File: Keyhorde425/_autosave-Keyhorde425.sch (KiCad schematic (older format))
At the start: 110 parts, among them J1 MX-NoLED, J2 USB_C_Receptacle_USB2.0, K1 MX-NoLED, M1 MX-NoLED, P1 MX-NoLED, Q1 MX-NoLED, SW1 SW_Push, T1 MX-NoLED, U1 ATmega32U4-AU, U2 MX-NoLED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

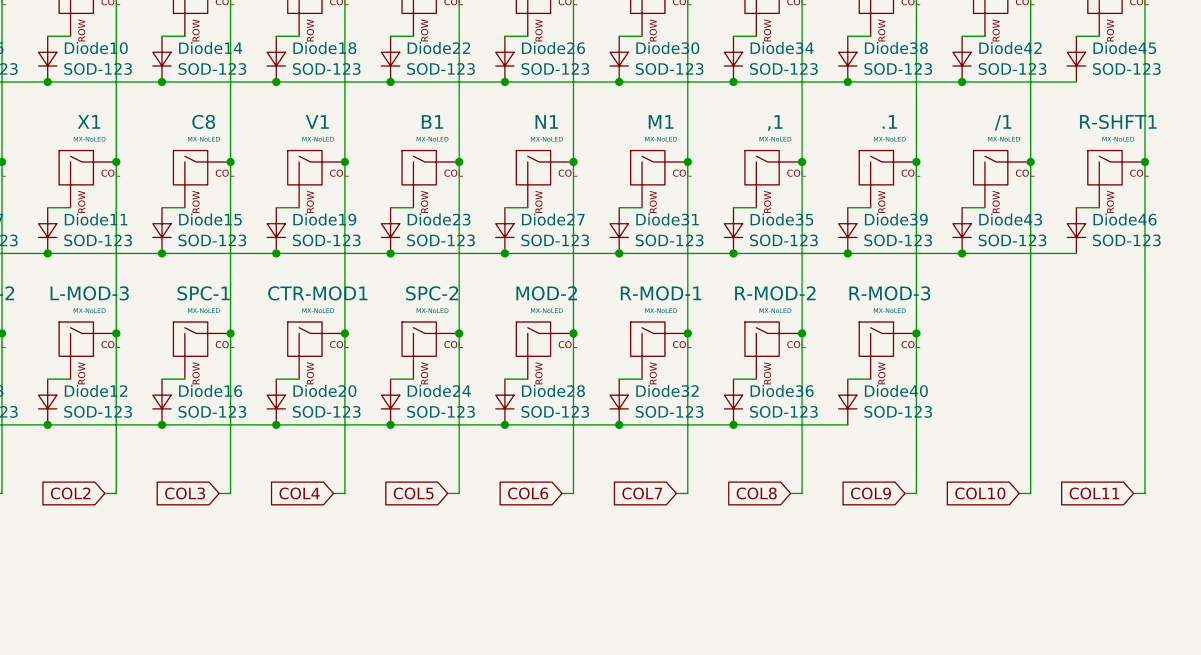
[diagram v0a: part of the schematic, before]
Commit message: Updated schematic with bad diode footprint
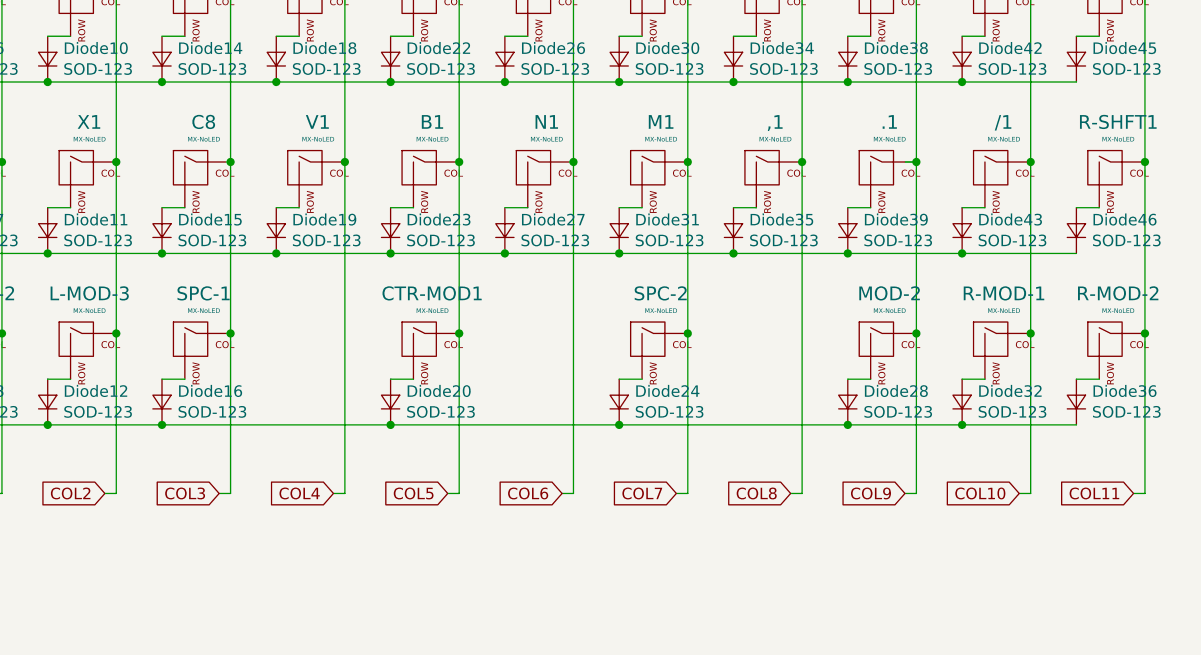
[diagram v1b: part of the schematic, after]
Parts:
- removed Diode40: SOD-123, Diode_THT:D_5KP_P7.62mm_Vertical_AnodeUp, symbol Device:D_Small
- removed R-MOD-3: MX-NoLED, MX_Alps_Hybrid:MX-1U, symbol MX_Alps_Hybrid:MX-NoLED
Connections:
- net COL10: now also R-MOD-1.1 (COL)
- net COL11: now also R-MOD-2.1 (COL)
- net COL4: no longer CTR-MOD1.1 (COL)
- net COL5: now also CTR-MOD1.1 (COL); no longer SPC-2.1 (COL)
- net COL6: no longer MOD-2.1 (COL)
- net COL7: now also SPC-2.1 (COL); no longer R-MOD-1.1 (COL)
- net COL8: no longer R-MOD-2.1 (COL)
- net COL9: now also MOD-2.1 (COL)
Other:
- moved on the sheet: CTR-MOD1, Diode20, Diode24, Diode28, Diode32, Diode36, MOD-2, R-MOD-1, R-MOD-2, SPC-2
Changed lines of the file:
@@
 L MX_Alps_Hybrid:MX-NoLED CTR-MOD1
 U 1 1 6388747C
-P 7250 4350
-F 0 "CTR-MOD1" H 7283 4573 60  0000 C CNN
-F 1 "MX-NoLED" H 7283 4499 20  0000 C CNN
-F 2 "MX_Alps_Hybrid:MX-1U" H 6625 4325 60  0001 C CNN
-F 3 "" H 6625 4325 60  0001 C CNN
-	1    7250 4350
-	1    0    0    -1
-$EndComp
-$Comp
-L Device:D_Small Diode20
-U 1 1 63887482
-P 7100 4600
-F 0 "Diode20" V 7146 4532 50  0000 R CNN
-F 1 "SOD-123" V 7055 4532 50  0000 R CNN
-F 2 "Diode_THT:D_5KP_P7.62mm_Vertical_AnodeUp" V 7100 4600 50  0001 C CNN
-F 3 "~" V 7100 4600 50  0001 C CNN
-	1    7100 4600
-	0    -1   -1   0
-$EndComp
-Wire Wire Line
-	7100 4500 7200 4500
-$Comp
-L MX_Alps_Hybrid:MX-NoLED SPC-2
-U 1 1 63887489
 P 7750 4350
-F 0 "SPC-2" H 7783 4573 60  0000 C CNN
+F 0 "CTR-MOD1" H 7783 4573 60  0000 C CNN
 F 1 "MX-NoLED" H 7783 4499 20  0000 C CNN
 F 2 "MX_Alps_Hybrid:MX-1U" H 7125 4325 60  0001 C CNN
@@
 $EndComp
 $Comp
-L Device:D_Small Diode24
-U 1 1 6388748F
+L Device:D_Small Diode20
+U 1 1 63887482
 P 7600 4600
-F 0 "Diode24" V 7646 4532 50  0000 R CNN
+F 0 "Diode20" V 7646 4532 50  0000 R CNN
 F 1 "SOD-123" V 7555 4532 50  0000 R CNN
 F 2 "Diode_THT:D_5KP_P7.62mm_Vertical_AnodeUp" V 7600 4600 50  0001 C CNN
@@
 	7600 4500 7700 4500
 $Comp
-L MX_Alps_Hybrid:MX-NoLED MOD-2
-U 1 1 63887496
-P 8250 4350
-F 0 "MOD-2" H 8283 4573 60  0000 C CNN
-F 1 "MX-NoLED" H 8283 4499 20  0000 C CNN
-F 2 "MX_Alps_Hybrid:MX-1U" H 7625 4325 60  0001 C CNN
-F 3 "" H 7625 4325 60  0001 C CNN
-	1    8250 4350
-	1    0    0    -1
-$EndComp
-$Comp
-L Device:D_Small Diode28
-U 1 1 6388749C
-P 8100 4600
-F 0 "Diode28" V 8146 4532 50  0000 R CNN
-F 1 "SOD-123" V 8055 4532 50  0000 R CNN
-F 2 "Diode_THT:D_5KP_P7.62mm_Vertical_AnodeUp" V 8100 4600 50  0001 C CNN
-F 3 "~" V 8100 4600 50  0001 C CNN
-	1    8100 4600
-	0    -1   -1   0
-$EndComp
-Wire Wire Line
-	8100 4500 8200 4500
-$Comp
-L MX_Alps_Hybrid:MX-NoLED R-MOD-1
-U 1 1 638874A3
+L MX_Alps_Hybrid:MX-NoLED SPC-2
+U 1 1 63887489
 P 8750 4350
-F 0 "R-MOD-1" H 8783 4573 60  0000 C CNN
+F 0 "SPC-2" H 8783 4573 60  0000 C CNN
 F 1 "MX-NoLED" H 8783 4499 20  0000 C CNN
 F 2 "MX_Alps_Hybrid:MX-1U" H 8125 4325 60  0001 C CNN
@@
 $EndComp
 $Comp
-L Device:D_Small Diode32
-U 1 1 638874A9
+L Device:D_Small Diode24
+U 1 1 6388748F
 P 8600 4600
-F 0 "Diode32" V 8646 4532 50  0000 R CNN
+F 0 "Diode24" V 8646 4532 50  0000 R CNN
 F 1 "SOD-123" V 8555 4532 50  0000 R CNN
 F 2 "Diode_THT:D_5KP_P7.62mm_Vertical_AnodeUp" V 8600 4600 50  0001 C CNN
@@
 	8600 4500 8700 4500
 $Comp
-L MX_Alps_Hybrid:MX-NoLED R-MOD-2
-U 1 1 638874B0
-P 9250 4350
-F 0 "R-MOD-2" H 9283 4573 60  0000 C CNN
-F 1 "MX-NoLED" H 9283 4499 20  0000 C CNN
-F 2 "MX_Alps_Hybrid:MX-1U" H 8625 4325 60  0001 C CNN
-F 3 "" H 8625 4325 60  0001 C CNN
-	1    9250 4350
-	1    0    0    -1
-$EndComp
-$Comp
-L Device:D_Small Diode36
-U 1 1 638874B6
-P 9100 4600
-F 0 "Diode36" V 9146 4532 50  0000 R CNN
-F 1 "SOD-123" V 9055 4532 50  0000 R CNN
-F 2 "Diode_THT:D_5KP_P7.62mm_Vertical_AnodeUp" V 9100 4600 50  0001 C CNN
-F 3 "~" V 9100 4600 50  0001 C CNN
-	1    9100 4600
-	0    -1   -1   0
-$EndComp
-Wire Wire Line
-	9100 4500 9200 4500
-$Comp
-L MX_Alps_Hybrid:MX-NoLED R-MOD-3
-U 1 1 638874BD
+L MX_Alps_Hybrid:MX-NoLED MOD-2
+U 1 1 63887496
 P 9750 4350
-F 0 "R-MOD-3" H 9783 4573 60  0000 C CNN
+F 0 "MOD-2" H 9783 4573 60  0000 C CNN
 F 1 "MX-NoLED" H 9783 4499 20  0000 C CNN
 F 2 "MX_Alps_Hybrid:MX-1U" H 9125 4325 60  0001 C CNN
@@
 $EndComp
 $Comp
-L Device:D_Small Diode40
-U 1 1 638874C3
+L Device:D_Small Diode28
+U 1 1 6388749C
 P 9600 4600
-F 0 "Diode40" V 9646 4532 50  0000 R CNN
+F 0 "Diode28" V 9646 4532 50  0000 R CNN
 F 1 "SOD-123" V 9555 4532 50  0000 R CNN
 F 2 "Diode_THT:D_5KP_P7.62mm_Vertical_AnodeUp" V 9600 4600 50  0001 C CNN
@@
 Wire Wire Line
 	9600 4500 9700 4500
+$Comp
+L MX_Alps_Hybrid:MX-NoLED R-MOD-1
+U 1 1 638874A3
+P 10250 4350
+F 0 "R-MOD-1" H 10283 4573 60  0000 C CNN
+F 1 "MX-NoLED" H 10283 4499 20  0000 C CNN
+F 2 "MX_Alps_Hybrid:MX-1U" H 9625 4325 60  0001 C CNN
+F 3 "" H 9625 4325 60  0001 C CNN
+	1    10250 4350
+	1    0    0    -1
+$EndComp
+$Comp
+L Device:D_Small Diode32
+U 1 1 638874A9
+P 10100 4600
+F 0 "Diode32" V 10146 4532 50  0000 R CNN
+F 1 "SOD-123" V 10055 4532 50  0000 R CNN
+F 2 "Diode_THT:D_5KP_P7.62mm_Vertical_AnodeUp" V 10100 4600 50  0001 C CNN
+F 3 "~" V 10100 4600 50  0001 C CNN
+	1    10100 4600
+	0    -1   -1   0
+$EndComp
+Wire Wire Line
+	10100 4500 10200 4500
 Wire Wire Line
 	5100 2450 5600 2450
@@
 Wire Wire Line
 	6100 4700 6600 4700
-Connection ~ 6600 4700
-Wire Wire Line
-	6600 4700 7100 4700
-Connection ~ 7100 4700
-Wire Wire Line
-	7100 4700 7600 4700
-Connection ~ 7600 4700
-Wire Wire Line
-	7600 4700 8100 4700
-Connection ~ 8100 4700
-Wire Wire Line
-	8100 4700 8600 4700
-Connection ~ 8600 4700
-Wire Wire Line
-	8600 4700 9100 4700
-Connection ~ 9100 4700
-Wire Wire Line
-	9100 4700 9600 4700
 Wire Wire Line
 	5400 2050 5400 2800
@@
 Wire Wire Line
 	7400 2800 7400 3550
-Connection ~ 7400 3550
-Wire Wire Line
-	7400 3550 7400 4300
 Wire Wire Line
 	7900 2050 7900 2800
@@
 Wire Wire Line
 	7900 2800 7900 3550
-Connection ~ 7900 3550
-Wire Wire Line
-	7900 3550 7900 4300
 Wire Wire Line
 	8400 2050 8400 2800
@@
 Wire Wire Line
 	8400 2800 8400 3550
-Connection ~ 8400 3550
-Wire Wire Line
-	8400 3550 8400 4300
 Wire Wire Line
 	8900 2050 8900 2800
@@
 Wire Wire Line
 	8900 2800 8900 3550
-Connection ~ 8900 3550
-Wire Wire Line
-	8900 3550 8900 4300
 Wire Wire Line
 	9400 2050 9400 2800
@@
 Wire Wire Line
 	9400 2800 9400 3550
-Connection ~ 9400 3550
-Wire Wire Line
-	9400 3550 9400 4300
 Wire Wire Line
 	9900 2050 9900 2800
@@
 Wire Wire Line
 	9900 2800 9900 3550
-Connection ~ 9900 3550
-Wire Wire Line
-	9900 3550 9900 4300
 Connection ~ 9100 2450
 Wire Wire Line
@@
 Connection ~ 6900 4300
 Wire Wire Line
-	7400 4300 7400 5000
-Wire Wire Line
 	7400 5000 7350 5000
-Connection ~ 7400 4300
-Wire Wire Line
-	7900 4300 7900 5000
 Wire Wire Line
 	7900 5000 7850 5000
-Connection ~ 7900 4300
-Wire Wire Line
-	8400 4300 8400 5000
 Wire Wire Line
 	8400 5000 8350 5000
-Connection ~ 8400 4300
-Wire Wire Line
-	8900 4300 8900 5000
 Wire Wire Line
 	8900 5000 8850 5000
-Connection ~ 8900 4300
-Wire Wire Line
-	9400 4300 9400 5000
 Wire Wire Line
 	9400 5000 9350 5000
-Connection ~ 9400 4300
-Wire Wire Line
-	9900 4300 9900 5000
 Wire Wire Line
 	9900 5000 9850 5000
-Connection ~ 9900 4300
-Wire Wire Line
-	10400 3550 10400 5000
+Wire Wire Line
+	10400 3550 10400 4300
 Wire Wire Line
 	10400 5000 10350 5000
 Connection ~ 10400 3550
-Wire Wire Line
-	10900 3550 10900 5000
 Wire Wire Line
 	10900 5000 10850 5000
@@
 Wire Wire Line
 	3600 3900 3850 3900
+Wire Wire Line
+	10900 3550 10900 4300
+Wire Wire Line
+	10600 4500 10700 4500
+$Comp
+L Device:D_Small Diode36
+U 1 1 638874B6
+P 10600 4600
+F 0 "Diode36" V 10646 4532 50  0000 R CNN
+F 1 "SOD-123" V 10555 4532 50  0000 R CNN
+F 2 "Diode_THT:D_5KP_P7.62mm_Vertical_AnodeUp" V 10600 4600 50  0001 C CNN
+F 3 "~" V 10600 4600 50  0001 C CNN
+	1    10600 4600
+	0    -1   -1   0
+$EndComp
+$Comp
+L MX_Alps_Hybrid:MX-NoLED R-MOD-2
+U 1 1 638874B0
+P 10750 4350
+F 0 "R-MOD-2" H 10783 4573 60  0000 C CNN
+F 1 "MX-NoLED" H 10783 4499 20  0000 C CNN
+F 2 "MX_Alps_Hybrid:MX-1U" H 10125 4325 60  0001 C CNN
+F 3 "" H 10125 4325 60  0001 C CNN
+	1    10750 4350
+	1    0    0    -1
+$EndComp
+Connection ~ 10900 4300
+Wire Wire Line
+	10900 4300 10900 5000
+Connection ~ 10400 4300
+Wire Wire Line
+	10400 4300 10400 5000
+Wire Wire Line
+	9850 3550 9900 3550
+Connection ~ 9900 3550
+Wire Wire Line
+	9900 3550 9900 4300
+Wire Wire Line
+	9900 4300 9900 5000
+Connection ~ 9900 4300
+Wire Wire Line
+	8900 3550 8900 4300
+Connection ~ 8900 3550
+Wire Wire Line
+	8900 4300 8900 5000
+Connection ~ 8900 4300
+Wire Wire Line
+	9400 3550 9400 5000
+Connection ~ 9400 3550
+Wire Wire Line
+	7900 3550 7900 4300
+Connection ~ 7900 3550
+Wire Wire Line
+	7900 4300 7900 5000
+Connection ~ 7900 4300
+Wire Wire Line
+	6600 4700 7600 4700
+Connection ~ 6600 4700
+Wire Wire Line
+	7600 4700 8600 4700
+Connection ~ 7600 4700
+Wire Wire Line
+	8600 4700 9600 4700
+Connection ~ 8600 4700
+Wire Wire Line
+	7400 3550 7400 5000
+Connection ~ 7400 3550
+Wire Wire Line
+	8400 3550 8400 5000
+Connection ~ 8400 3550
+Wire Wire Line
+	9600 4700 10100 4700
+Connection ~ 9600 4700
+Wire Wire Line
+	10100 4700 10600 4700
+Connection ~ 10100 4700
 $EndSCHEMATC
